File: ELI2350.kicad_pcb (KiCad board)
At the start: 4 copper layers, 155 x 103 mm, 56 parts, among them J3 Conn_01x03_Pin, U1 W25Q128JVPIQ, U2 FLASH or PSRAM, U3 TPS62163DSG, U4 TLV76733DRVR, U5 RP235x-B, U6 TLV76733DRVR, Y1 CM4012M00012001

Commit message: alpha
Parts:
- added H1: MountingHole_Pad, MountingHole:MountingHole_2.2mm_M2_Pad, F.Cu at (145.3, 85.8)
- added H2: MountingHole_Pad, MountingHole:MountingHole_2.2mm_M2_Pad, F.Cu at (145.4, 54.3)
- J3, U2: moved to B.Cu
- moved CN2 65.0 mm to (155.9, 84.3), turned to 0 degrees
- moved CN3 58.5 mm to (163.1, 84.3), turned to 0 degrees
- moved C21 46.2 mm to (163.2, 55.6)
- moved C22 46.2 mm to (158.0, 54.8)
- moved U6 46.2 mm to (160.6, 56.2)
- moved J3 43.6 mm to (158.4, 57.0), turned to 90 degrees
- moved CN1 41.7 mm to (185.9, 69.4), turned to -90 degrees
- moved C36 40.6 mm to (152.2, 79.9)
- moved R3 39.4 mm to (152.3, 78.3), turned to 180 degrees
- moved USB1 37.9 mm to (149.0, 64.4), turned to -90 degrees
- moved R19 35.1 mm to (152.7, 67.8)
- moved R18 35.0 mm to (154.4, 64.3)
- moved R8 31.0 mm to (167.5, 85.4), turned to -90 degrees
- moved R21 30.9 mm to (149.9, 85.2)
- moved C37 30.2 mm to (165.4, 62.0)
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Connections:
- CN2 pad 2: /GPIO1 -> GND
- CN3 pad 1: /GPIO20 -> /GPIO21
- CN3 pad 2: /GPIO21 -> GND
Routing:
- net /USB_D-: track 7.35 -> 95.8 mm, vias 2 -> 0
- net +12V: track 0.00 -> 86.0 mm, vias 0 -> 4
- net /USB_D+: track 7.55 -> 93.5 mm, vias 2 -> 0
- net /GPIO33: track 0.00 -> 80.3 mm, vias 0 -> 3
- net /GPIO21: track 0.00 -> 60.8 mm, vias 0 -> 5
- net /GPIO0: track 0.00 -> 59.6 mm, vias 0 -> 4
- net /~{RESET}: track 4.23 -> 62.6 mm, vias 0 -> 4
- net /GPIO22: track 0.00 -> 47.6 mm, vias 0 -> 4
- net /+3V3_SIG: track 19.1 -> 66.7 mm, vias 0 -> 3
- net /GPIO23: track 0.00 -> 46.9 mm, vias 0 -> 4
- net /GPIO15: track 0.00 -> 45.2 mm, vias 0 -> 4
- net /GPIO19: track 30.9 -> 74.6 mm, vias 0 -> 6
- net /GPIO14: track 0.00 -> 43.4 mm, vias 0 -> 4
- net /GPIO11: track 0.00 -> 42.8 mm, vias 0 -> 4
- net /GPIO47: track 0.00 -> 40.2 mm, vias 0 -> 2
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- added copper zone on F.Cu, net +12V
- added copper zone on F.Cu, net Net-(U3-SW)
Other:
- board size 155 x 103 mm -> 50.9 x 37.1 mm
- board text removed: "MIDI In"

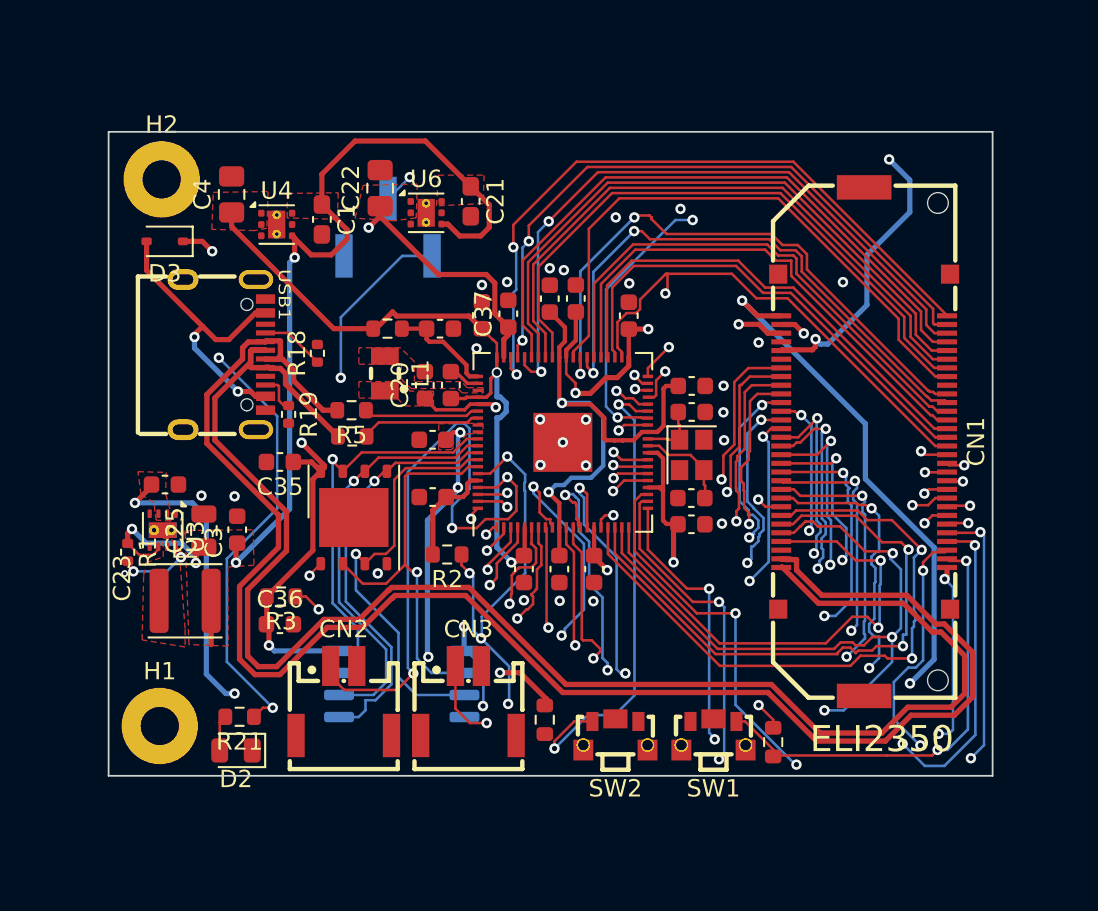
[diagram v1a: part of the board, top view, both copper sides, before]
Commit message: dock and near finished compute board
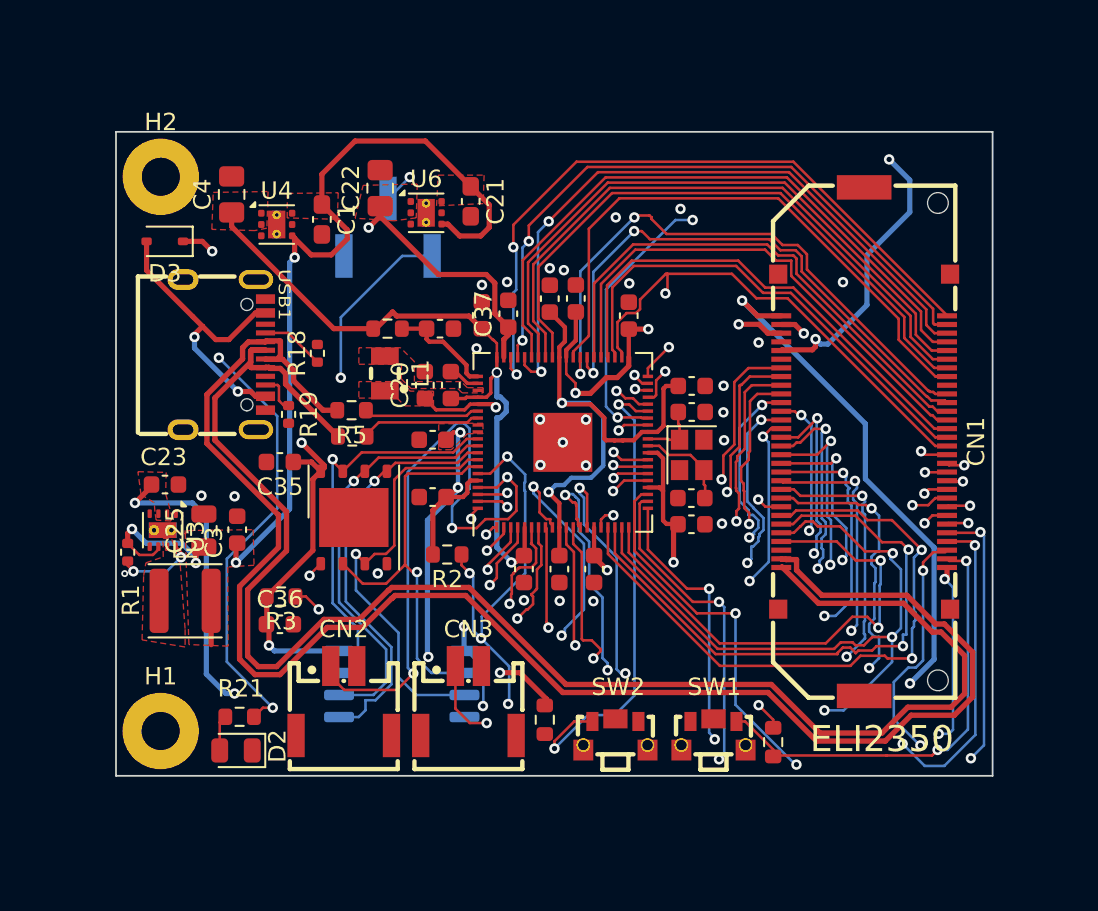
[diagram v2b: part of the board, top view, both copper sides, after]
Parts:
- removed kibuzzard-6695C28C: G***, kibuzzard-6695C28C
- moved H1 0.29 mm to (145.3, 86.1)
- moved H2 0.16 mm to (145.3, 54.1)
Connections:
- H2 pad 1: unconnected-(H2-Pad1) -> GND
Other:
- board size 50.9 x 37.1 mm -> 50.5 x 37.1 mm
- board text added: "ELI2350a Nov 2025 Emute Lab Instruments"
- board text removed: "12mHz"

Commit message: doc pre-reroute
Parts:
- added TP1: TestPoint, TestPoint:TestPoint_Pad_1.5x1.5mm, B.Cu at (189.3, 85.1)
- added TP2: TestPoint, TestPoint:TestPoint_Pad_1.5x1.5mm, B.Cu at (183.6, 61.6)
- added TP3: TestPoint, TestPoint:TestPoint_Pad_1.5x1.5mm, B.Cu at (162.0, 66.2)
- added TP4: TestPoint, TestPoint:TestPoint_Pad_1.5x1.5mm, B.Cu at (165.9, 53.8)
- added TP5: TestPoint, TestPoint:TestPoint_Pad_1.5x1.5mm, B.Cu at (158.7, 67.9)
- added TP6: TestPoint, TestPoint:TestPoint_Pad_1.5x1.5mm, B.Cu at (177.1, 76.0)
- moved R3 0.61 mm to (152.9, 78.3)
- moved R1 0.13 mm to (143.5, 75.7)
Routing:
- net /GPIO19: track 74.6 -> 92.7 mm
- net +3V3: track 147.6 -> 154.6 mm
- net /GPIO20: track 29.0 -> 35.7 mm
- net +1.1V: track 38.3 -> 44.5 mm
- net /+3V3_SIG: track 66.7 -> 69.9 mm, vias 3 -> 4
- net +5V: track 97.9 -> 100.5 mm
- net /GPIO2: track 26.1 -> 28.4 mm
- net +12V: track 86.0 -> 88.1 mm
- net /GPIO8: track 36.9 -> 38.8 mm
- net /QSPI_SCLK: track 24.1 -> 22.2 mm
- net /GPIO9: track 37.7 -> 36.2 mm
- net /~{QSPI_CS_{0}}: track 53.5 -> 55.0 mm
- net /GPIO13: track 38.6 -> 37.3 mm
- net /GPIO15: track 45.2 -> 43.9 mm
- net /GPIO25: track 23.4 -> 24.6 mm
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- added copper zone on In2.Cu, net GND
- removed copper zone on In2.Cu, net +3V3

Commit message: bboard
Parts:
- removed SW2: ~, emutelab:KEY-SMD_SKTDLHE010
- added SW3: ~, emutelab:SW-SMD_4P-L3.5-W2.9-P1.30-LS4.8, F.Cu at (176.0, 86.0)
- C23: footprint Capacitor_SMD:C_0603_1608Metric -> Capacitor_SMD:C_0805_2012Metric
- SW1: footprint emutelab:KEY-SMD_SKTDLHE010 -> emutelab:SW-SMD_4P-L3.5-W2.9-P1.30-LS4.8
- moved D2 29.4 mm to (158.3, 59.1), turned to 0 degrees
- moved R21 26.6 mm to (160.7, 60.9)
- moved U3 17.2 mm to (157.4, 86.9), turned to 0 degrees
- moved R1 17.2 mm to (158.0, 85.0), turned to 180 degrees
- moved C23 17.0 mm to (154.4, 86.5), turned to -90 degrees
- moved CN3 16.8 mm to (146.3, 84.9), turned to -90 degrees
- moved L2 16.4 mm to (161.6, 85.5), turned to 90 degrees
- moved H1 14.6 mm to (144.6, 71.5)
- moved C3 13.3 mm to (160.5, 82.4), turned to 0 degrees
- moved C25 13.0 mm to (157.3, 83.4), turned to 180 degrees
- moved CN2 11.6 mm to (146.3, 77.8), turned to -90 degrees
- moved R8 9.36 mm to (159.9, 79.9), turned to 0 degrees
- moved SW1 7.45 mm to (169.7, 86.0), turned to 0 degrees
- moved R18 2.95 mm to (152.2, 62.3)
- moved USB1 1.95 mm to (147.1, 63.8)
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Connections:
- SW1 pad 1: /~{BOOTSEL} -> unconnected-(SW1-Pad1)
- SW1 pad 2: GND -> /~{RESET}
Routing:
- net /GPIO33: track 80.3 -> 40.7 mm, vias 3 -> 2
- net /GPIO19: track 92.7 -> 72.1 mm
- net +12V: track 88.1 -> 72.9 mm, vias 4 -> 3
- net /GPIO21: track 61.0 -> 75.4 mm
- net /GPIO0: track 59.5 -> 46.0 mm, vias 4 -> 3
- net +3V3: track 154.6 -> 144.5 mm, vias 13 -> 12
- net /GPIO20: track 35.7 -> 28.0 mm
- net +5V: track 100.5 -> 107.9 mm
- net /GPIO22: track 47.6 -> 54.3 mm
- net /~{QSPI_CS_{0}}: track 55.0 -> 48.5 mm
- net /~{RESET}: track 62.8 -> 69.2 mm
- net /~{BOOTSEL}: track 26.1 -> 30.5 mm
- net Net-(U3-PG): track 4.66 -> 1.52 mm, vias 2 -> 0
- net /GPIO5: track 30.8 -> 28.9 mm
- net /GPIO18: track 36.2 -> 34.3 mm
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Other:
- board size 50.5 x 37.1 mm -> 51.4 x 37.1 mm
- board text added: "BSEL"
- board text added: "ELI2350b May 2026 Emute Lab Instruments"
- board text added: "RESET"
- board text removed: "ELI2350a Nov 2025 Emute Lab Instruments"
